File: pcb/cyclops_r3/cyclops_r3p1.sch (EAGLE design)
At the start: 48 parts, among them Q1 SUM11006, Q2 IRF510, U1 MCP4921, U2 317-N, U3 ADR03, U4 OP1177, U5 LM324N

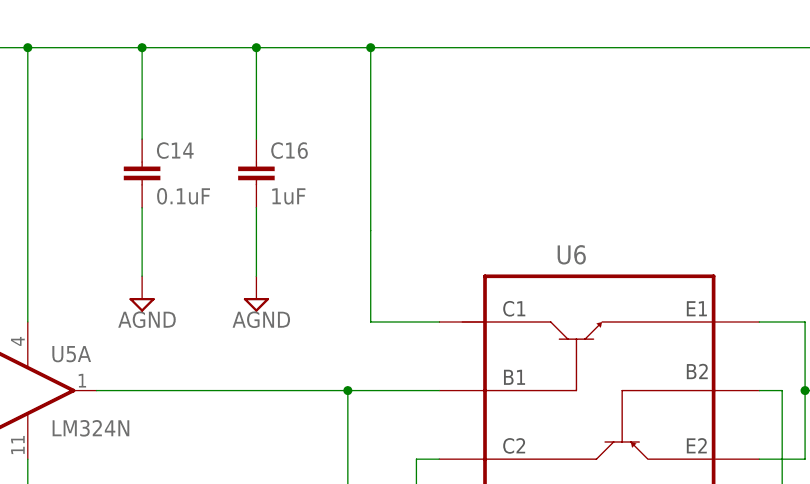
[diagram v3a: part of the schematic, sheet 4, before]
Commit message: Added NMOS bias network to the layout.
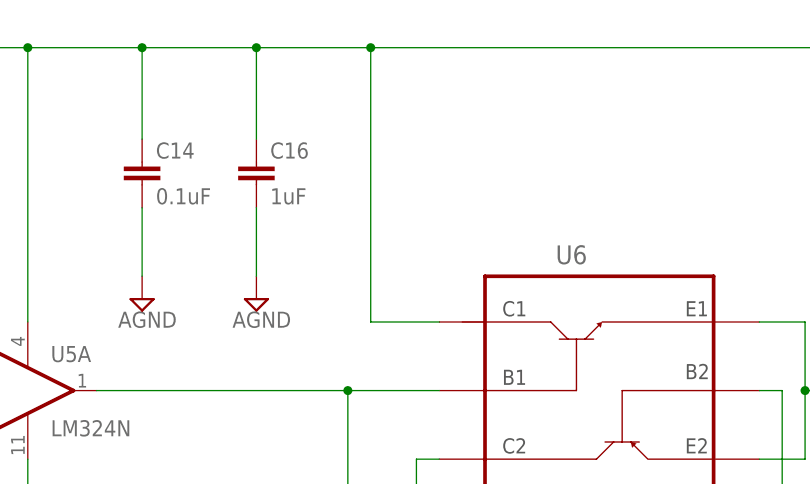
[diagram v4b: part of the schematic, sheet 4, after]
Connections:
- removed net AGND: R11.1
- removed net N$12: U6.C1
- net +12V: now also U6.C1
- net GND: now also R11.1
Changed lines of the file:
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@@
 <wire x1="71.12" y1="76.2" x2="73.66" y2="76.2" width="0.1524" layer="91"/>
+</segment>
+<segment>
+<pinref part="SUPPLY1" gate="G$1" pin="AGND"/>
+<pinref part="R11" gate="R" pin="1"/>
+<wire x1="134.62" y1="48.26" x2="134.62" y2="66.04" width="0.1524" layer="91"/>
 </segment>
 </net>
@@
 <wire x1="53.34" y1="121.92" x2="66.04" y2="121.92" width="0.1524" layer="91"/>
 <junction x="53.34" y="121.92"/>
-<wire x1="66.04" y1="101.6" x2="66.04" y2="121.92" width="0.1524" layer="91"/>
+<wire x1="66.04" y1="91.44" x2="66.04" y2="121.92" width="0.1524" layer="91"/>
 <wire x1="66.04" y1="121.92" x2="134.62" y2="121.92" width="0.1524" layer="91"/>
 <junction x="66.04" y="121.92"/>
@@
 <wire x1="134.62" y1="101.6" x2="134.62" y2="121.92" width="0.1524" layer="91"/>
 <junction x="134.62" y="121.92"/>
+<pinref part="U6" gate="G$1" pin="C1"/>
+<wire x1="73.66" y1="91.44" x2="66.04" y2="91.44" width="0.1524" layer="91"/>
 </segment>
 </net>
@@
 </segment>
 </net>
-<net name="N$12" class="1">
-<segment>
-<pinref part="U6" gate="G$1" pin="C1"/>
-<wire x1="66.04" y1="91.44" x2="73.66" y2="91.44" width="0.1524" layer="91"/>
-<wire x1="66.04" y1="101.6" x2="66.04" y2="91.44" width="0.1524" layer="91"/>
-</segment>
-</net>
 <net name="N$13" class="0">
 <segment>
@@
 </segment>
 </net>
-<net name="AGND" class="0">
-<segment>
-<pinref part="SUPPLY1" gate="G$1" pin="AGND"/>
-<pinref part="R11" gate="R" pin="1"/>
-<wire x1="134.62" y1="48.26" x2="134.62" y2="66.04" width="0.1524" layer="91"/>
-</segment>
-</net>

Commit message: Not too sure what I did here, to be honest.
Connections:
- net +5V: now also U$1.5V
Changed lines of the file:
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@@
 <wire x1="231.14" y1="71.12" x2="231.14" y2="45.72" width="0.1524" layer="91"/>
+</segment>
+<segment>
+<pinref part="U$1" gate="G$1" pin="5V"/>
+<wire x1="58.42" y1="17.78" x2="58.42" y2="12.7" width="0.1524" layer="91"/>
 </segment>
 </net>
@@
 <net name="+15V" class="1">
 <segment>
+<pinref part="I/O_BLOCK" gate="G$1" pin="1"/>
+<wire x1="43.18" y1="-5.08" x2="68.58" y2="-5.08" width="0.1524" layer="91"/>
 <label x="50.8" y="-5.08" size="1.778" layer="95"/>
 </segment>
-<segment>
-<pinref part="I/O_BLOCK" gate="G$1" pin="1"/>
-<wire x1="43.18" y1="-5.08" x2="68.58" y2="-5.08" width="0.1524" layer="91"/>
-</segment>
 </net>

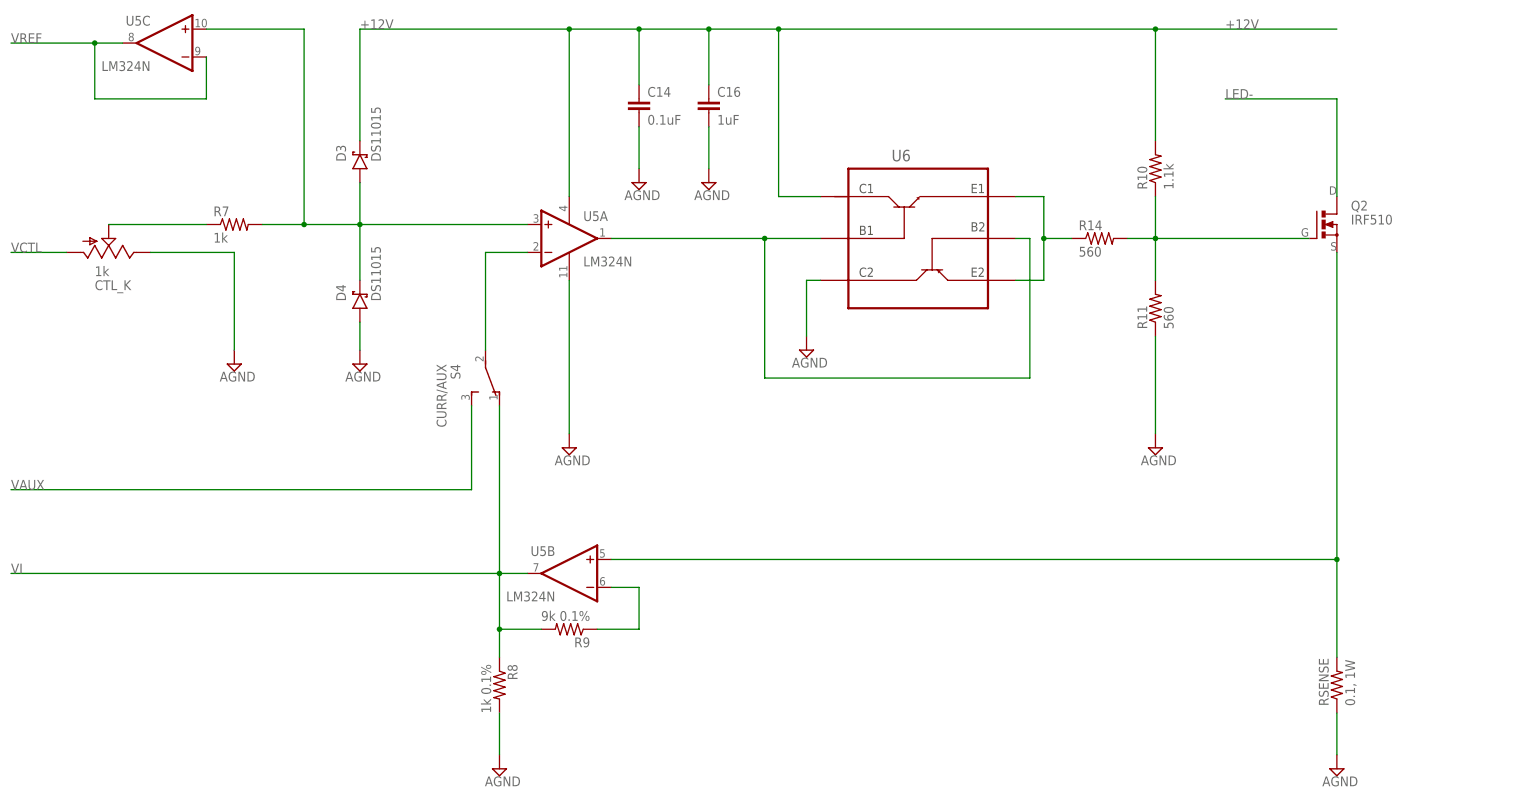
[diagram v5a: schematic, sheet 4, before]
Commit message: The board is pretty much finished. I need to verify a few components and add a bottom silkscreen with detailed board info before fabrication, though. Also, there are some ERC issues that are not really problems, but should be fixed on the schematic for perfection's sake.
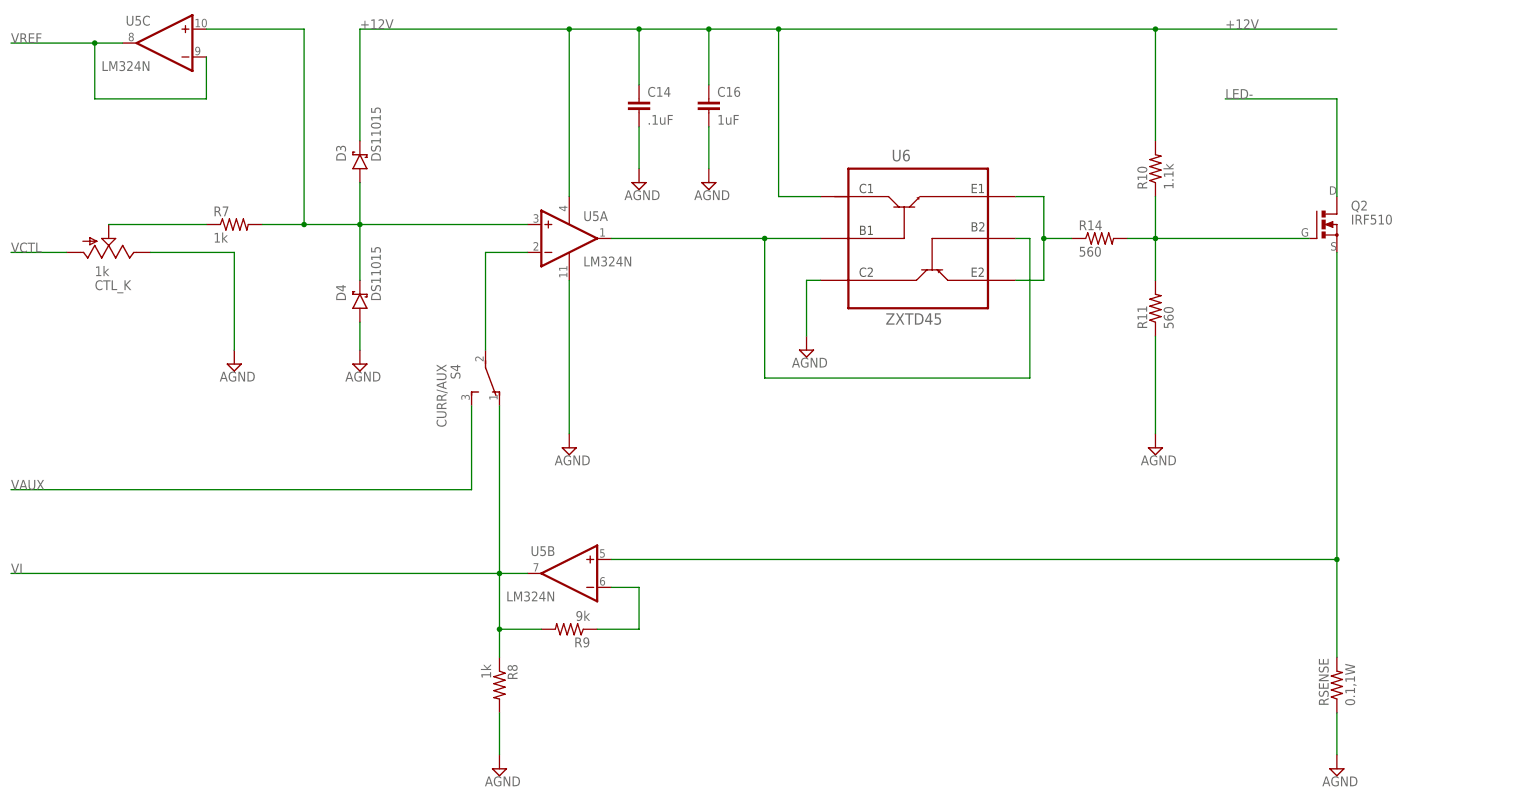
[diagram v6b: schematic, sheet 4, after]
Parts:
- C12, C13, C14, C3: value 0.1uF -> .1uF
- D1: value MMSZ5240B -> MMSZ
- D2: value S1B-13-F -> S1B
- R8: value 1k 0.1% -> 1k
- R9: value 9k 0.1% -> 9k
- RSENSE: value 0.1, 1W -> 0.1,1W
- U6: value (none) -> ZXTD45
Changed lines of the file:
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@@
 <part name="U$1" library="cyclops" deviceset="ARDUINO_R3_ICSP" device=""/>
 <part name="U2" library="cyclops" deviceset="*317" device="_TO263" value="317-N"/>
-<part name="D2" library="cyclops" deviceset="DIODE" device="S1B-13-F" value="S1B-13-F"/>
+<part name="D2" library="cyclops" deviceset="DIODE" device="S1B-13-F" value="S1B"/>
 <part name="R3" library="cyclops" deviceset="R" device="_0603" value="1.8k"/>
 <part name="R4" library="cyclops" deviceset="R" device="_0603" value="240k"/>
@@
 <part name="P+2" library="cyclops" deviceset="+5V" device=""/>
 <part name="C2" library="cyclops" deviceset="C" device="_0805" value="10uF"/>
-<part name="C3" library="cyclops" deviceset="C" device="_0603" value="0.1uF"/>
+<part name="C3" library="cyclops" deviceset="C" device="_0603" value=".1uF"/>
 <part name="C4" library="cyclops" deviceset="C" device="_0805" value="1uF"/>
 <part name="SUPPLY13" library="cyclops" deviceset="AGND" device=""/>
@@
 <part name="R1" library="cyclops" deviceset="R" device="_0603" value="??"/>
 <part name="SUPPLY16" library="cyclops" deviceset="AGND" device=""/>
-<part name="R9" library="cyclops" deviceset="R" device="_0603" value="9k 0.1%"/>
-<part name="R8" library="cyclops" deviceset="R" device="_0603" value="1k 0.1%"/>
-<part name="RSENSE" library="cyclops" deviceset="R" device="_2512" value="0.1, 1W"/>
+<part name="R9" library="cyclops" deviceset="R" device="_0603" value="9k"/>
+<part name="R8" library="cyclops" deviceset="R" device="_0603" value="1k"/>
+<part name="RSENSE" library="cyclops" deviceset="R" device="_2512" value="0.1,1W"/>
 <part name="U3" library="cyclops" deviceset="ADR03AKSZ-REEL7" device="" value="ADR03"/>
 <part name="C10" library="cyclops" deviceset="C" device="_0805" value="1uF"/>
-<part name="C12" library="cyclops" deviceset="C" device="_0603" value="0.1uF"/>
+<part name="C12" library="cyclops" deviceset="C" device="_0603" value=".1uF"/>
 <part name="SUPPLY5" library="cyclops" deviceset="AGND" device=""/>
 <part name="SUPPLY6" library="cyclops" deviceset="AGND" device=""/>
@@
 <part name="R2" library="cyclops" deviceset="R" device="_0603" value="10k"/>
 <part name="SUPPLY20" library="cyclops" deviceset="AGND" device=""/>
-<part name="D1" library="cyclops" deviceset="Z-DIODE" device="_MMSZ" value="MMSZ5240B"/>
+<part name="D1" library="cyclops" deviceset="Z-DIODE" device="_MMSZ" value="MMSZ"/>
 <part name="SUPPLY2" library="cyclops" deviceset="AGND" device=""/>
 <part name="SUPPLY22" library="cyclops" deviceset="AGND" device=""/>
@@
 <part name="R6" library="cyclops" deviceset="R" device="_0603" value="1k"/>
 <part name="C16" library="cyclops" deviceset="C" device="_0805" value="1uF"/>
-<part name="C14" library="cyclops" deviceset="C" device="_0603" value="0.1uF"/>
+<part name="C14" library="cyclops" deviceset="C" device="_0603" value=".1uF"/>
 <part name="SUPPLY30" library="cyclops" deviceset="AGND" device=""/>
 <part name="D4" library="cyclops" deviceset="S-DIODE" device="SOD-123" value="DS11015"/>
@@
 <part name="SUPPLY33" library="cyclops" deviceset="AGND" device=""/>
 <part name="S1" library="cyclops" deviceset="SPDT" device="_PCM12" value="INPUT SRC"/>
-<part name="C13" library="cyclops" deviceset="C" device="_0603" value="0.1uF"/>
+<part name="C13" library="cyclops" deviceset="C" device="_0603" value=".1uF"/>
 <part name="C11" library="cyclops" deviceset="C" device="_0805" value="1uF"/>
 <part name="C7" library="cyclops" deviceset="C-POL" device="_0807" value="47uF"/>
@@
 <part name="SUPPLY34" library="cyclops" deviceset="GND" device=""/>
 <part name="S3" library="cyclops" deviceset="SPDT" device="_CFPA" value="TEST"/>
-<part name="U6" library="cyclops" deviceset="ZXTD4591E6" device=""/>
+<part name="U6" library="cyclops" deviceset="ZXTD4591E6" device="" value="ZXTD45"/>
 <part name="SUPPLY35" library="cyclops" deviceset="AGND" device=""/>
 <part name="Q2" library="cyclops" deviceset="N-MOSFET" device="TO-262" value="IRF510"/>
